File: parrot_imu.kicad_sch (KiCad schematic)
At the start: 29 parts, among them J1 Conn_01x02_Male, J3 TB005-762-02BE, U1 TR05S3V3, U2 VR10S05, U3 Spark_fun_ICM-20948, U4 Teensy4.1, U5 TJA1441AT/0Z, U6 ESDCAN24-2BLY

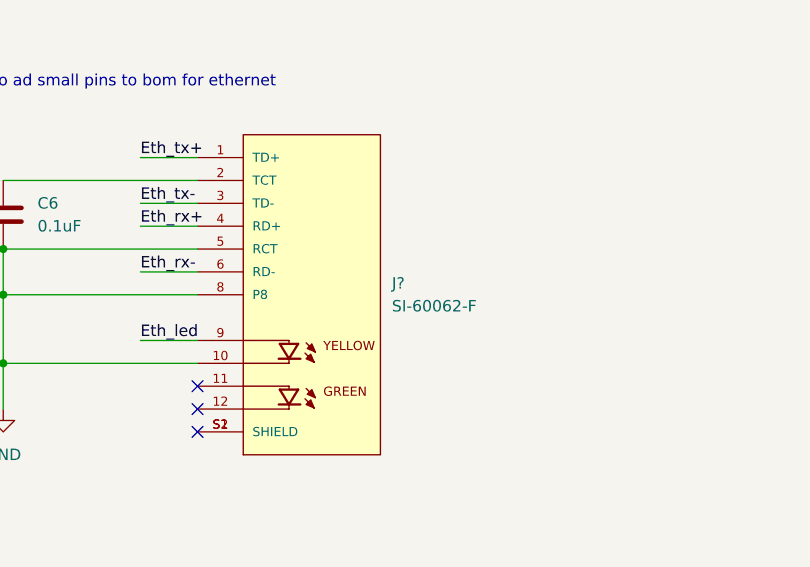
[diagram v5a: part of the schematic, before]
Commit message: start of laying out components
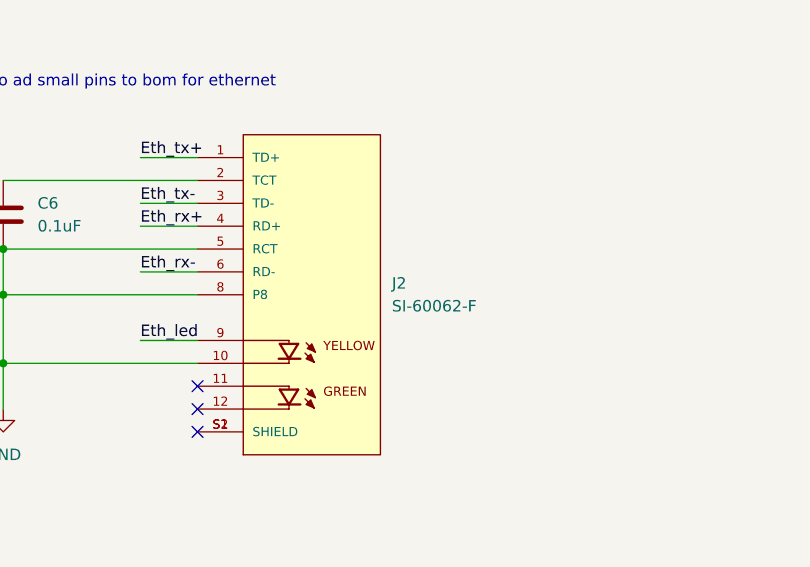
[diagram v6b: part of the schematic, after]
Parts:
- gave numbers to parts that had none: 1
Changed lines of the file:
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@@
   (symbol (lib_id "SI-60062-F:SI-60062-F") (at 313.69 163.83 0) (unit 1)
     (in_bom yes) (on_board yes) (fields_autoplaced)
-    (property "Reference" "J?" (id 0) (at 322.58 162.5599 0)
+    (property "Reference" "J2" (id 0) (at 322.58 162.5599 0)
       (effects (font (size 1.27 1.27)) (justify left))
     )
@@
       (reference "J1") (unit 1) (value "Conn_01x02_Male") (footprint "Connector_AMASS:AMASS_XT30PW-M_1x02_P2.50mm_Horizontal")
     )
+    (path "/0d20f8ee-a6f7-49a8-87a9-065aa3be88a2"
+      (reference "J2") (unit 1) (value "SI-60062-F") (footprint "magjack:BEL_SI-60062-F")
+    )
     (path "/3048e5f9-287c-4759-b62e-bdb281c9ffef"
       (reference "J3") (unit 1) (value "TB005-762-02BE") (footprint "connector_parrot:CUI_TB005-762-02BE")
     )
-    (path "/0d20f8ee-a6f7-49a8-87a9-065aa3be88a2"
-      (reference "J?") (unit 1) (value "SI-60062-F") (footprint "magjack:BEL_SI-60062-F")
-    )
     (path "/b80ac4e5-0546-4f4a-ab29-51df51ca7732"

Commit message: most of pcb and some steps
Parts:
- J1: footprint Connector_AMASS:AMASS_XT30PW-M_1x02_P2.50mm_Horizontal -> Connector_AMASS:AMASS_XT30PW-F_1x02_P2.50mm_Horizontal
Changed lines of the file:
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@@
       (effects (font (size 1.27 1.27)) (justify right))
     )
-    (property "Footprint" "Connector_AMASS:AMASS_XT30PW-M_1x02_P2.50mm_Horizontal" (id 2) (at 34.29 129.54 0)
+    (property "Footprint" "Connector_AMASS:AMASS_XT30PW-F_1x02_P2.50mm_Horizontal" (id 2) (at 34.29 129.54 0)
       (effects (font (size 1.27 1.27)) hide)
     )
@@
     )
     (path "/35ca6dd5-0fe6-4149-b1eb-072213388a9c"
-      (reference "J1") (unit 1) (value "Conn_01x02_Male") (footprint "Connector_AMASS:AMASS_XT30PW-M_1x02_P2.50mm_Horizontal")
+      (reference "J1") (unit 1) (value "Conn_01x02_Male") (footprint "Connector_AMASS:AMASS_XT30PW-F_1x02_P2.50mm_Horizontal")
     )
     (path "/0d20f8ee-a6f7-49a8-87a9-065aa3be88a2"

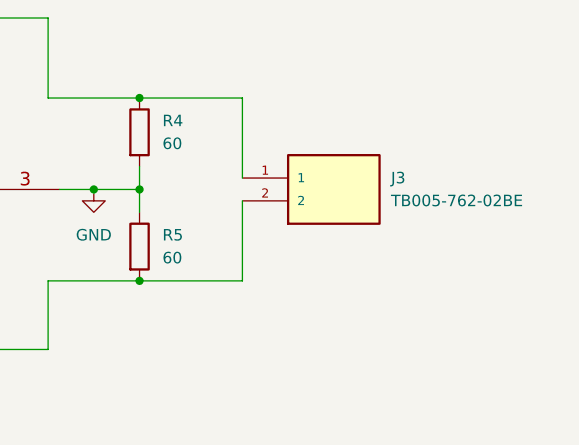
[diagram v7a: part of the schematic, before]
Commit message: completed draft pcb and added model for imu
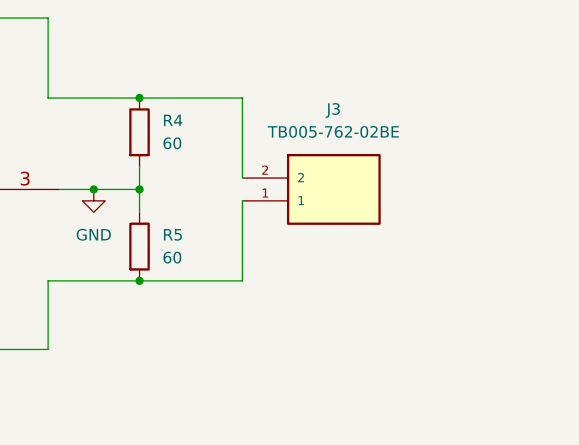
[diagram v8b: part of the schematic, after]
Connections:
- net at R4.1, U5.7 (CANH), U6.1: now also J3.2; no longer J3.1
- net at R5.2, U5.6 (CANL), U6.2: now also J3.1; no longer J3.2
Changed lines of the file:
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@@
     (pin "3")
   )
-  (symbol (lib_id "connector_parrot:TB005-762-02BE") (at 382.27 62.23 0) (unit 1)
+  (symbol (lib_id "connector_parrot:TB005-762-02BE") (at 382.27 59.69 0) (mirror x) (unit 1)
     (in_bom yes) (on_board yes) (fields_autoplaced)
-    (property "Reference" "J3" (id 0) (at 388.62 59.6899 0)
-      (effects (font (size 1.27 1.27)) (justify left))
-    )
-    (property "Value" "TB005-762-02BE" (id 1) (at 388.62 62.2299 0)
-      (effects (font (size 1.27 1.27)) (justify left))
-    )
-    (property "Footprint" "connector_parrot:CUI_TB005-762-02BE" (id 2) (at 382.27 62.23 0)
+    (property "Reference" "J3" (id 0) (at 382.27 52.07 0))
+    (property "Value" "TB005-762-02BE" (id 1) (at 382.27 54.61 0))
+    (property "Footprint" "connector_parrot:CUI_TB005-762-02BE" (id 2) (at 382.27 59.69 0)
       (effects (font (size 1.27 1.27)) (justify bottom) hide)
     )
-    (property "Datasheet" "" (id 3) (at 382.27 62.23 0)
+    (property "Datasheet" "" (id 3) (at 382.27 59.69 0)
       (effects (font (size 1.27 1.27)) hide)
     )
-    (property "MANUFACTURER" "CUI" (id 4) (at 382.27 62.23 0)
+    (property "MANUFACTURER" "CUI" (id 4) (at 382.27 59.69 0)
       (effects (font (size 1.27 1.27)) (justify bottom) hide)
     )
-    (property "STANDARD" "Manufacturer Recommendations" (id 5) (at 382.27 62.23 0)
+    (property "STANDARD" "Manufacturer Recommendations" (id 5) (at 382.27 59.69 0)
       (effects (font (size 1.27 1.27)) (justify bottom) hide)
     )
-    (property "Digikey" "102-6189-ND" (id 6) (at 382.27 62.23 0)
+    (property "Digikey" "102-6189-ND" (id 6) (at 382.27 59.69 0)
       (effects (font (size 1.27 1.27)) hide)
     )
